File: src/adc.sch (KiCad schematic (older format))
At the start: 29 parts, among them P2 CONN_01X15, P3 CONN_01X03, U10 LM741, U11 LM311N, U7 LM741, U8 DG444, U9 LM741

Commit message: update
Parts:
- added C314: C, Capacitors_ThroughHole:C_Radial_D7.5_L11.2_P2.5, symbol C
- C311: renamed from C13; footprint (none) -> Capacitors_SMD:C_1206
- R16: footprint (none) -> Resistors_ThroughHole:Resistor_TO-220_Vertical
- R301: renamed from R14; footprint Resistors_SMD:R_1206 -> Resistors_ThroughHole:Resistor_TO-220_Vertical
- R302: renamed from R15; footprint Resistors_SMD:R_1206 -> Resistors_ThroughHole:Resistor_TO-220_Vertical
- R304: renamed from R17; footprint (none) -> Resistors_SMD:R_1206
- R305: renamed from R18; footprint (none) -> Resistors_SMD:R_1206
- R306: renamed from R19; footprint (none) -> Resistors_SMD:R_1206
- U304: renamed from U10; footprint (none) -> Housings_SOIC:SOIC-8_3.9x4.9mm_Pitch1.27mm
- U305: renamed from U11; footprint (none) -> Housings_SOIC:SOIC-8_3.9x4.9mm_Pitch1.27mm
- U8: footprint (none) -> Housings_SOIC:SOIC-16_3.9x9.9mm_Pitch1.27mm
- U9: footprint (none) -> Housings_SOIC:SOIC-8_3.9x4.9mm_Pitch1.27mm
- W301: renamed from W1; footprint (none) -> Pin_Headers:Pin_Header_Straight_1x01
- renumbered C14 to C301, C15 to C302, C16 to C303, C17 to C304, C18 to C305, C19 to C306, C20 to C307, C21 to C308, C22 to C309, C23 to C310, C24 to C312, C25 to C313, D5 to D301, D6 to D302, P2 to P301, P3 to P302, U7 to U301
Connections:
- net at C311.2, R16.1, U8.14 (S3)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: now also C314.2
- net at C311.1, P302.1 (P1), U304.3 (+)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: now also C314.1
- net GND renamed 0V
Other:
- moved on the sheet: C311

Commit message: complete
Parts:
- C314: footprint Capacitors_ThroughHole:C_Radial_D7.5_L11.2_P2.5 -> Capacitors_ThroughHole:C_Rect_L7_W3.5_P5
- D301, D302: footprint Diodes_ThroughHole:Diode_DO-35_SOD27_Horizontal_RM10 -> Diodes_SMD:MiniMELF_Standard
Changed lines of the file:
@@
 F 0 "D301" H 7775 3325 40  0000 L BNN
 F 1 "1N4148" H 7725 3175 40  0000 L CNN
-F 2 "Diodes_ThroughHole:Diode_DO-35_SOD27_Horizontal_RM10" H 7850 3400 30  0001 C CNN
+F 2 "Diodes_SMD:MiniMELF_Standard" H 7850 3400 30  0001 C CNN
 F 3 "" H 7850 3250 60  0000 C CNN
 	1    7850 3250
@@
 F 0 "D302" H 7775 3625 40  0000 L BNN
 F 1 "1N4148" H 7725 3475 40  0000 L CNN
-F 2 "Diodes_ThroughHole:Diode_DO-35_SOD27_Horizontal_RM10" H 7850 3700 30  0001 C CNN
+F 2 "Diodes_SMD:MiniMELF_Standard" H 7850 3700 30  0001 C CNN
 F 3 "" H 7850 3550 60  0000 C CNN
 	1    7850 3550
@@
 F 0 "C314" H 6175 3100 50  0000 L CNN
 F 1 "C" H 6175 2900 50  0000 L CNN
-F 2 "Capacitors_ThroughHole:C_Radial_D7.5_L11.2_P2.5" H 6188 2850 50  0001 C CNN
+F 2 "Capacitors_ThroughHole:C_Rect_L7_W3.5_P5" H 6188 2850 50  0001 C CNN
 F 3 "" H 6150 3000 50  0000 C CNN
 	1    6150 3000

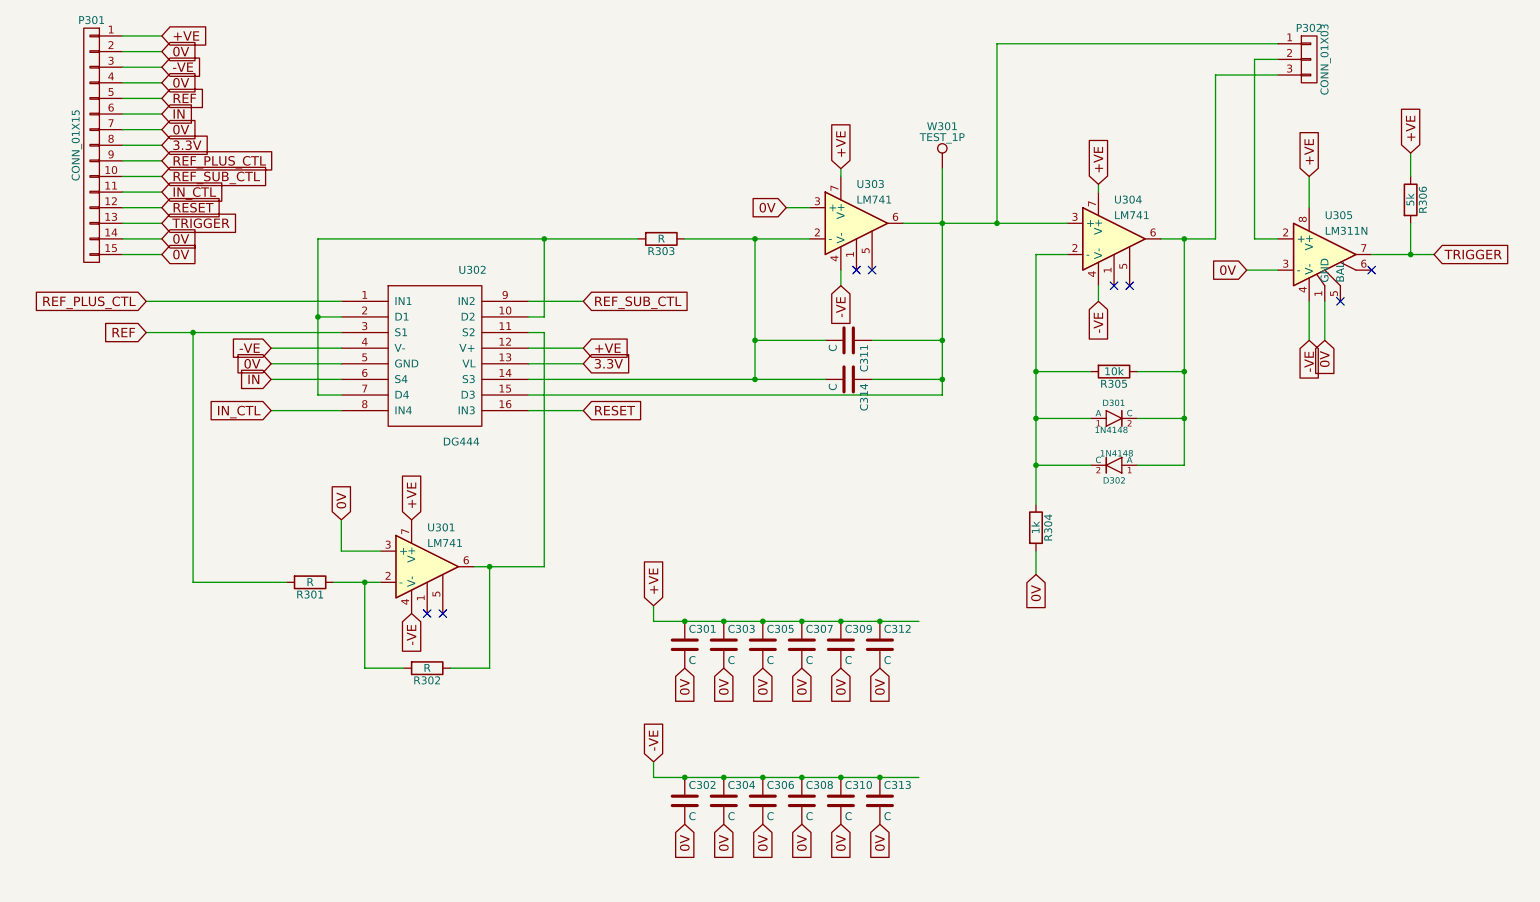
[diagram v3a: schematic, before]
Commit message: change schematic from 0V to AGND
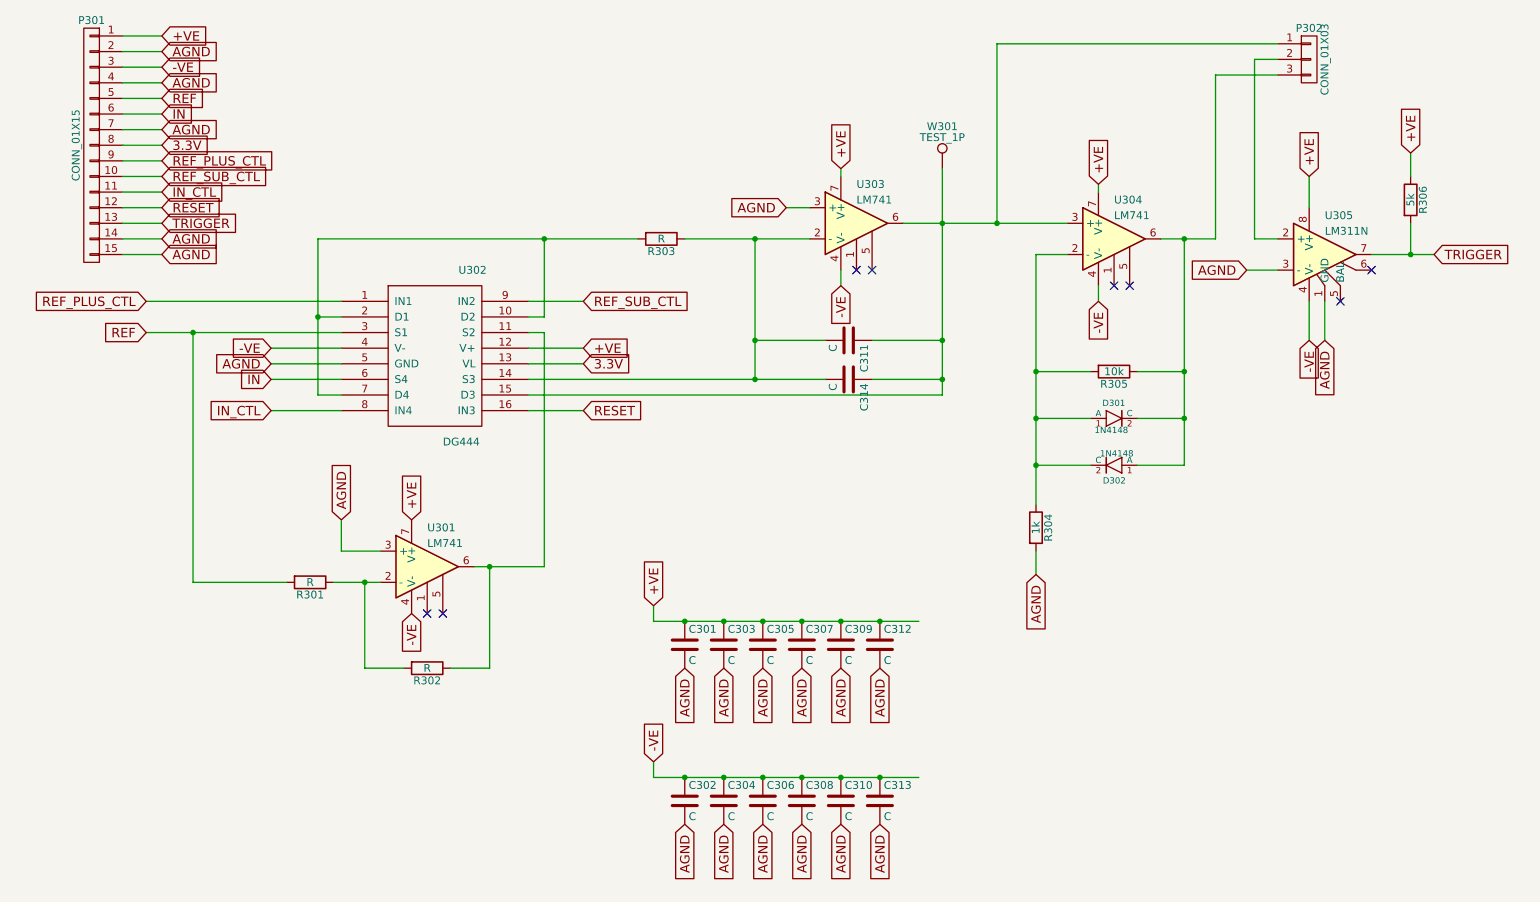
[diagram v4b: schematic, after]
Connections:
- net 0V renamed AGND
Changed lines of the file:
@@
 $EndComp
 Text GLabel 2450 2900 0    60   Input ~ 0
-0V
+AGND
 Text GLabel 1750 800  2    60   Input ~ 0
 +VE
 Text GLabel 1750 900  2    60   Input ~ 0
-0V
+AGND
 Text GLabel 1750 1000 2    60   Input ~ 0
 -VE
@@
 $EndComp
 Text GLabel 5750 1900 0    60   Input ~ 0
-0V
+AGND
 Text GLabel 2450 3200 0    60   Input ~ 0
 IN_CTL
@@
 NoConn ~ 3550 4500
 Text GLabel 2900 3900 1    60   Input ~ 0
-0V
+AGND
 Text GLabel 1650 2500 0    60   Input ~ 0
 REF_PLUS_CTL
@@
 $EndComp
 Text GLabel 1750 1100 2    60   Input ~ 0
-0V
+AGND
 Text GLabel 1750 1400 2    60   Input ~ 0
-0V
+AGND
 $Comp
 L LM741 U304
@@
 $EndComp
 Text GLabel 7350 4250 3    60   Input ~ 0
-0V
+AGND
 Text GLabel 7750 1750 1    60   Input ~ 0
 +VE
@@
 $EndComp
 Text GLabel 1750 2100 2    60   Input ~ 0
-0V
+AGND
 Text GLabel 1750 2200 2    60   Input ~ 0
-0V
+AGND
 $Comp
 L TEST_1P W301
@@
 $EndComp
 Text GLabel 8700 2300 0    60   Input ~ 0
-0V
+AGND
 Text GLabel 9100 1700 1    60   Input ~ 0
 +VE
@@
 -VE
 Text GLabel 9200 2750 3    60   Input ~ 0
-0V
+AGND
 Text GLabel 9900 2200 2    60   Input ~ 0
 TRIGGER
@@
 Connection ~ 5100 4550
 Text GLabel 5100 4850 3    60   Input ~ 0
-0V
+AGND
 $Comp
 L C C303
@@
 Connection ~ 5350 4550
 Text GLabel 5350 4850 3    60   Input ~ 0
-0V
+AGND
 Connection ~ 5600 4550
 Text GLabel 5600 4850 3    60   Input ~ 0
-0V
+AGND
 $Comp
 L C C302
@@
 Connection ~ 5100 5550
 Text GLabel 5100 5850 3    60   Input ~ 0
-0V
+AGND
 $Comp
 L C C304
@@
 Connection ~ 5350 5550
 Text GLabel 5350 5850 3    60   Input ~ 0
-0V
+AGND
 Connection ~ 5600 5550
 Text GLabel 5600 5850 3    60   Input ~ 0
-0V
+AGND
 Text GLabel 4900 5450 1    60   Input ~ 0
 -VE
@@
 Connection ~ 5850 4550
 Text GLabel 5850 4850 3    60   Input ~ 0
-0V
+AGND
 $Comp
 L C C309
@@
 Connection ~ 6100 4550
 Text GLabel 6100 4850 3    60   Input ~ 0
-0V
+AGND
 Connection ~ 6350 4550
 Text GLabel 6350 4850 3    60   Input ~ 0
-0V
+AGND
 $Comp
 L C C308
@@
 Connection ~ 5850 5550
 Text GLabel 5850 5850 3    60   Input ~ 0
-0V
+AGND
 $Comp
 L C C310
@@
 Connection ~ 6100 5550
 Text GLabel 6100 5850 3    60   Input ~ 0
-0V
+AGND
 Connection ~ 6350 5550
 Text GLabel 6350 5850 3    60   Input ~ 0
-0V
+AGND
 $Comp
 L R R306
